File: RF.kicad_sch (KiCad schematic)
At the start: 31 parts, among them J4 SMA (2.4GHz), J5 SMA (2.4GHz), J6 U.FL-R-SMT-1(80), U10 MAX-M10S, U5 RFX2401C, U6 2450BM14A0002T, U7 2450BP39D100CE, U8 nRF24L01P, U9 E220-400M30S, Y1 ECS-160-9-33B-CTP-TR

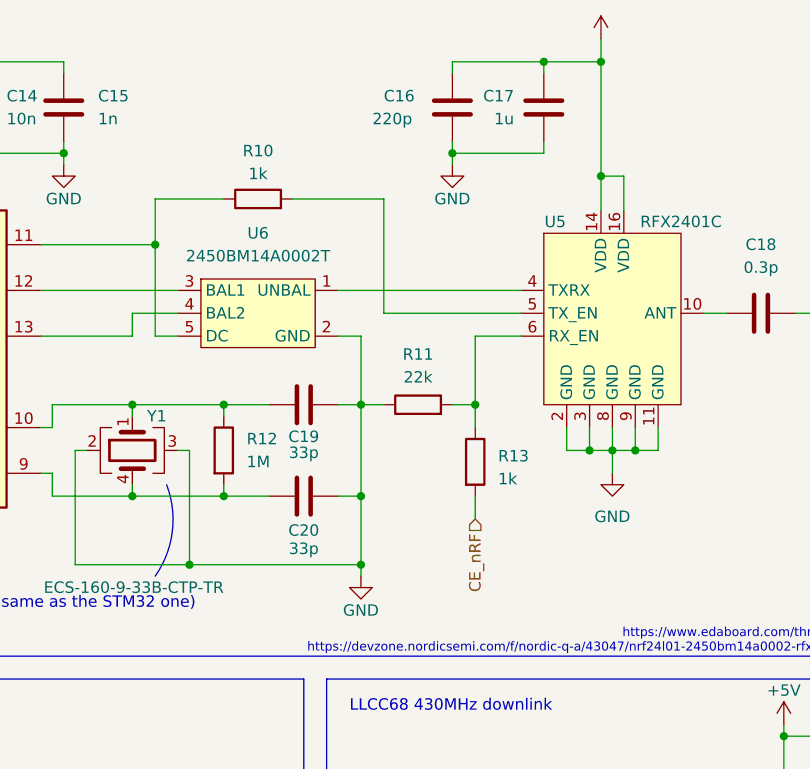
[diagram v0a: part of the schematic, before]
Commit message: :building_construction: Simplify power circuit and consolidate BOM
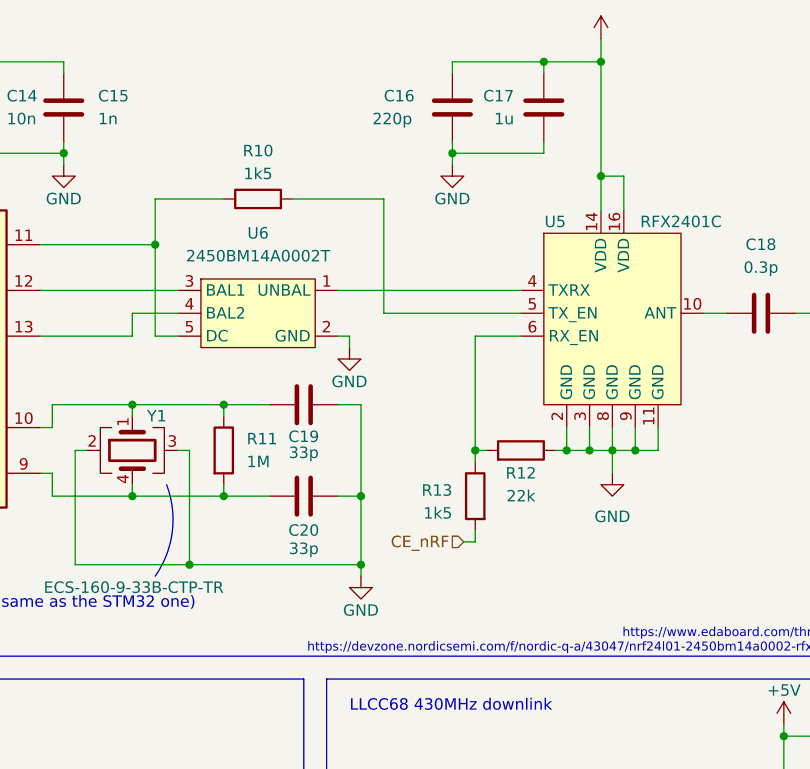
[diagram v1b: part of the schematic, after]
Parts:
- removed R11: 22k, Resistor_SMD:R_0402_1005Metric_Pad0.72x0.64mm_HandSolder, symbol Device:R
- added R12: 22k, Resistor_SMD:R_0402_1005Metric_Pad0.72x0.64mm_HandSolder, symbol Device:R
- R10, R13: value 1k -> 1k5
- renumbered R12 to R11
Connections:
- net GND: now also R12.1
- net at R13.1, U5.6 (RX_EN): now also R12.2
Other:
- moved on the sheet: R13

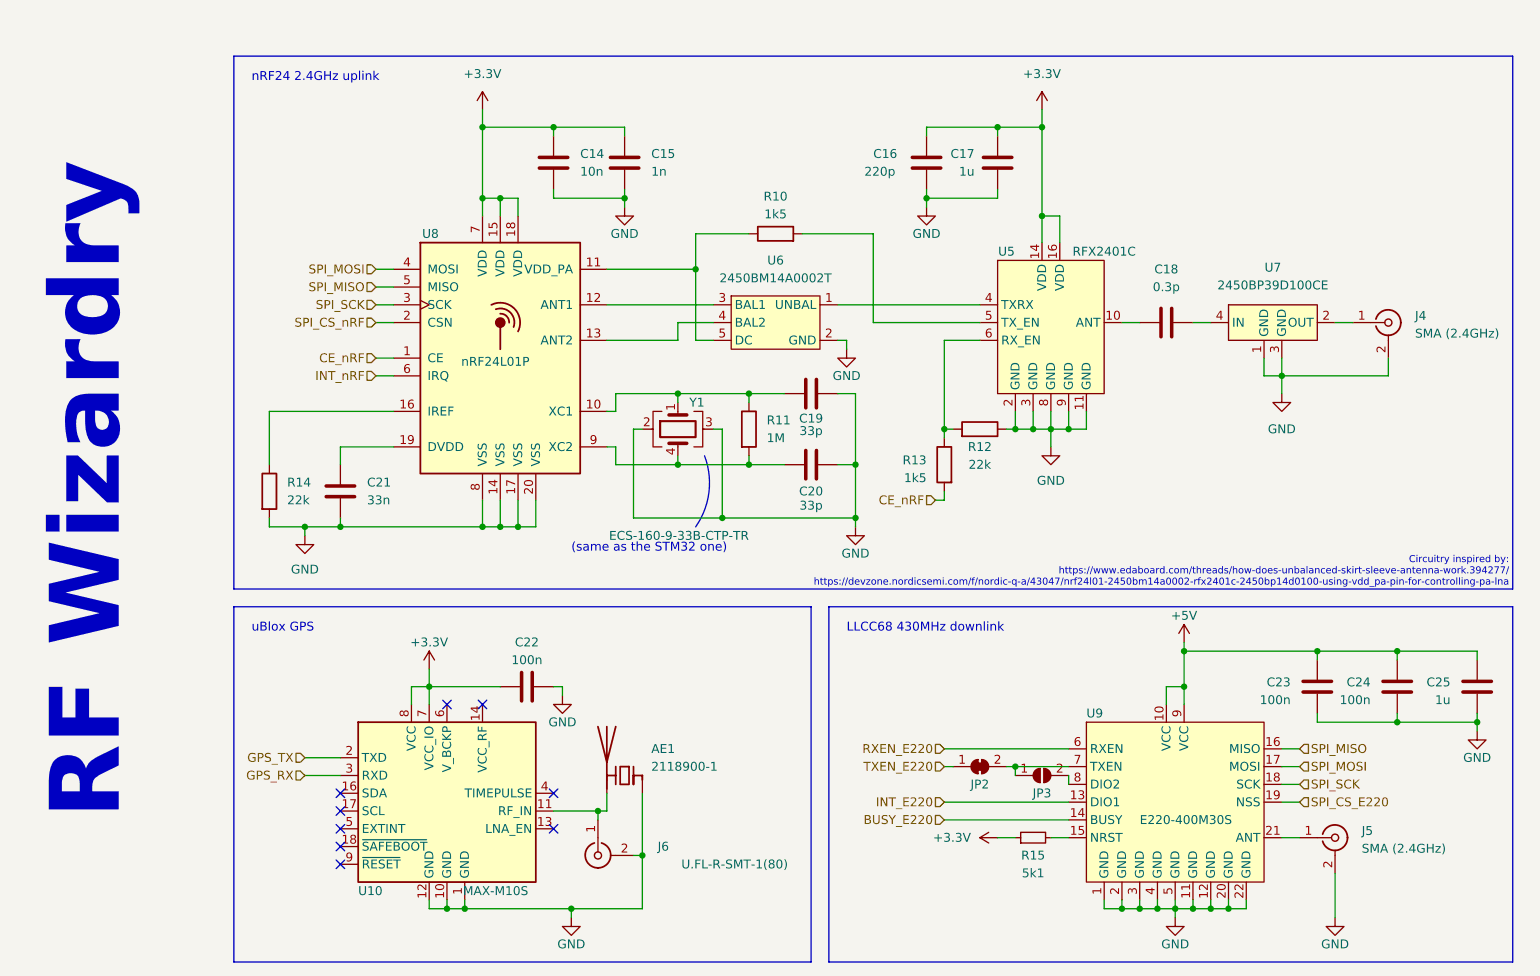
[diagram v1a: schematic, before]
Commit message: :building_construction: Replace debug header with TagConnect and inline STM32 decoupling caps
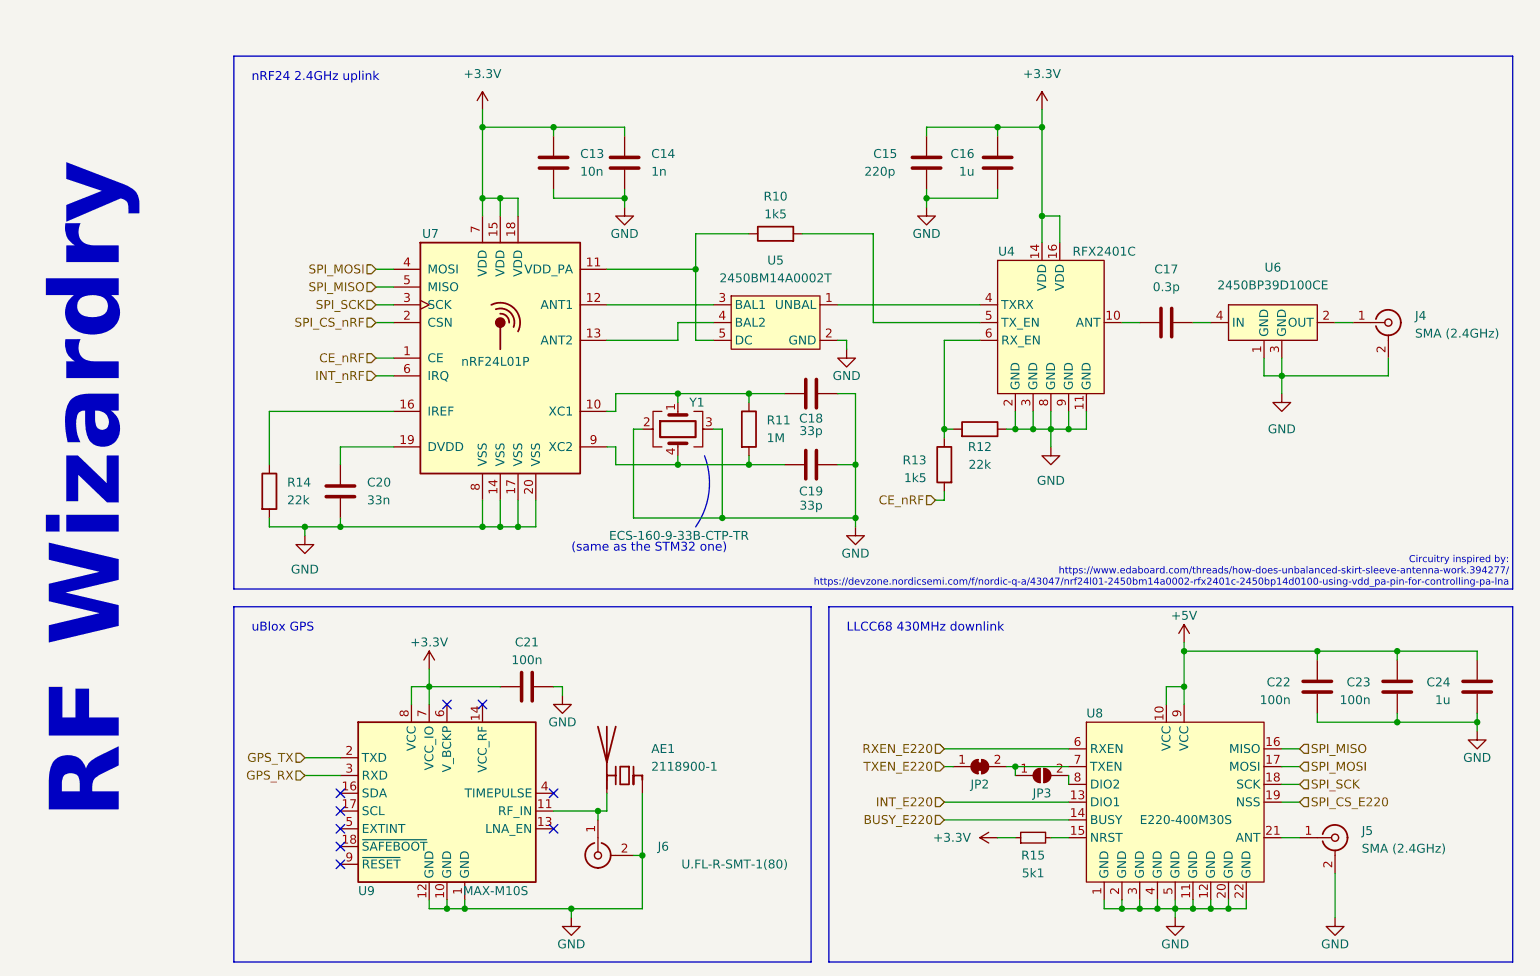
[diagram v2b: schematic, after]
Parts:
- renumbered C14 to C13, C15 to C14, C16 to C15, C17 to C16, C18 to C17, C19 to C18, C20 to C19, C21 to C20, C22 to C21, C23 to C22, C24 to C23, C25 to C24, U5 to U4, U6 to U5, U7 to U6, U8 to U7, U9 to U8, U10 to U9

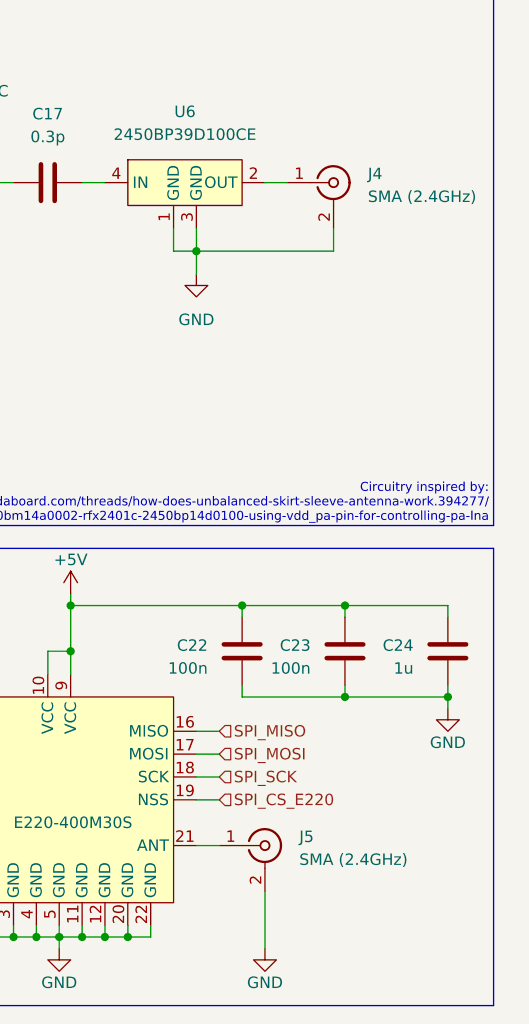
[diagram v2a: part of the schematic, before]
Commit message: :bug: Simplify SMA connector BOM value
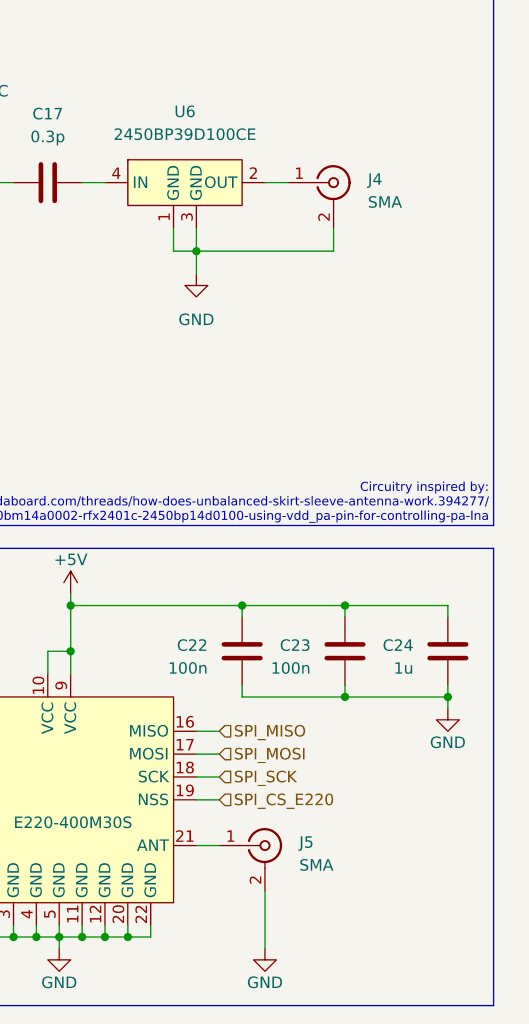
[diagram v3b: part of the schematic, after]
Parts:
- J4, J5: value SMA (2.4GHz) -> SMA
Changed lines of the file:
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@@
   (symbol (lib_id "Connector:Conn_Coaxial") (at 217.17 139.7 0) (unit 1)
     (in_bom yes) (on_board yes) (dnp no) (fields_autoplaced)
-    (property "Reference" "J5" (at 220.98 138.7231 0)
-      (effects (font (size 1.27 1.27)) (justify left))
-    )
-    (property "Value" "SMA (2.4GHz)" (at 220.98 141.2631 0)
+    (property "Reference" "J5" (at 220.98 139.3582 0)
+      (effects (font (size 1.27 1.27)) (justify left))
+    )
+    (property "Value" "SMA" (at 220.98 141.8982 0)
       (effects (font (size 1.27 1.27)) (justify left))
     )
@@
   (symbol (lib_id "Connector:Conn_Coaxial") (at 224.79 66.04 0) (unit 1)
     (in_bom yes) (on_board yes) (dnp no) (fields_autoplaced)
-    (property "Reference" "J4" (at 228.6 65.0631 0)
-      (effects (font (size 1.27 1.27)) (justify left))
-    )
-    (property "Value" "SMA (2.4GHz)" (at 228.6 67.6031 0)
-      (effects (font (size 1.27 1.27)) (justify left))
-    )
+    (property "Reference" "J4" (at 228.6 65.6982 0)
+      (effects (font (size 1.27 1.27)) (justify left))
+    )
+    (property "Value" "SMA" (at 228.6 68.2382 0)
+      (effects (font (size 1.27 1.27)) (justify left))
+    )
